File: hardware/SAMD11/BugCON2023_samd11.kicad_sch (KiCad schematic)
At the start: 26 parts, among them J1 Conn_01x04_Pin, J2 Conn_01x04_Pin, J3 Conn_01x02, P1 USB_C_Plug_USB2.0, Q1 DMG3415U-7, SW1 SW_Push, SW2 ON, U1 ATSAMD11C14A-SS, U2 AP2112K-3.3

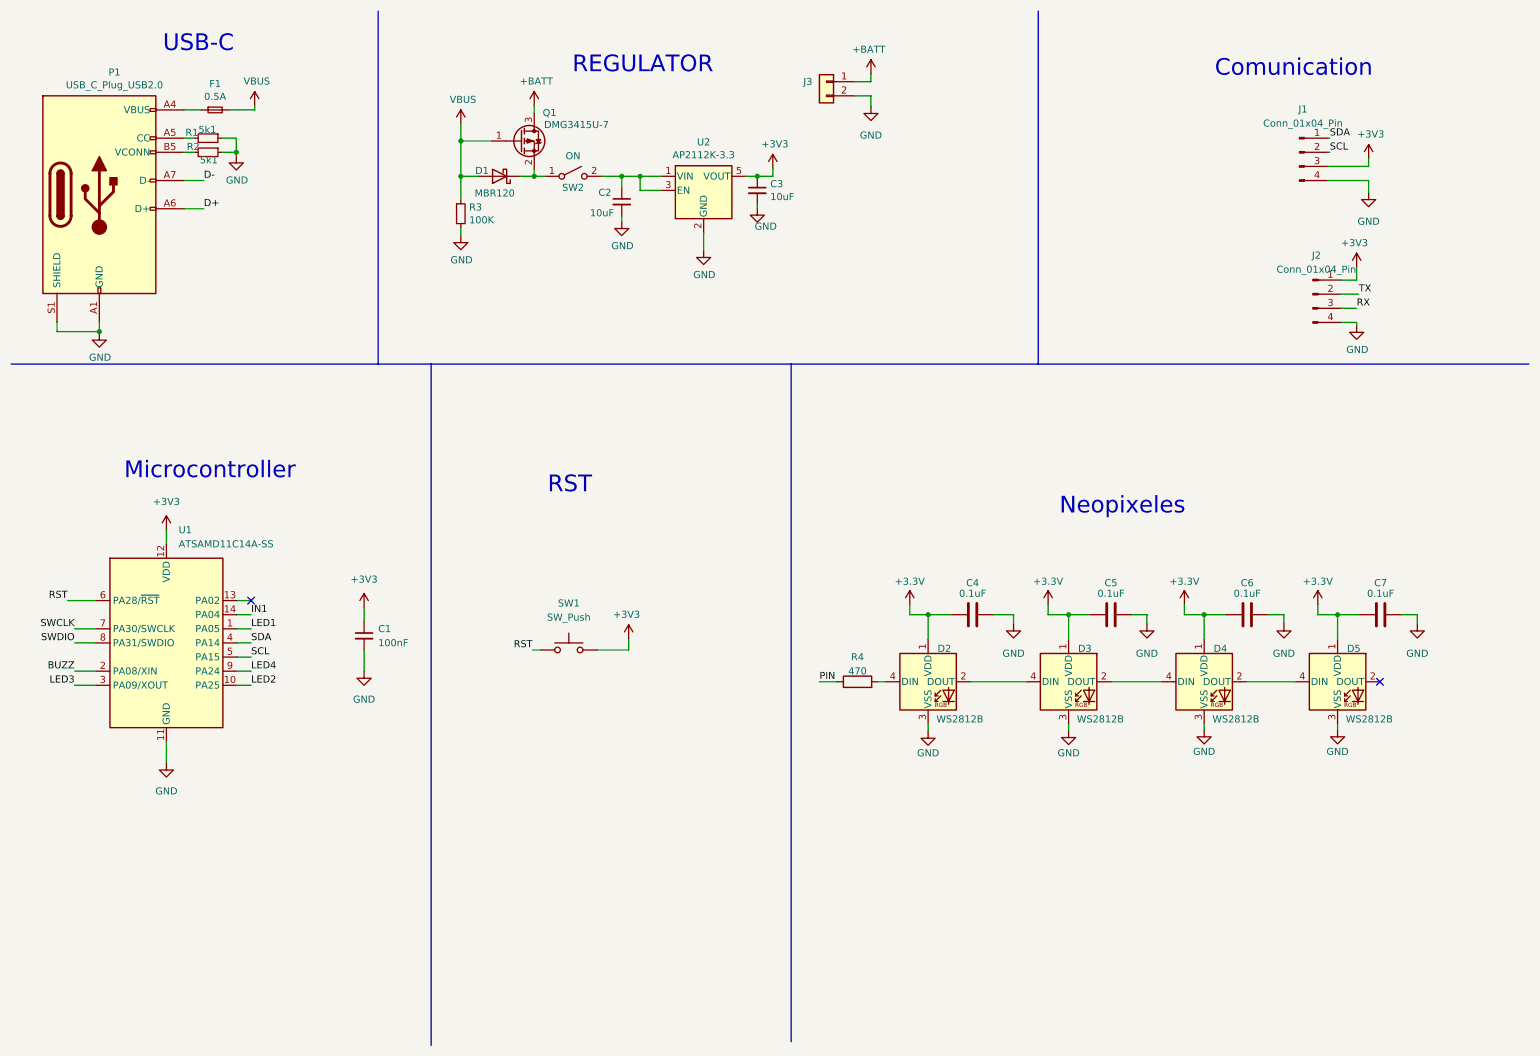
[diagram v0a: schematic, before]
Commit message: add pcb size, footprints & 3D
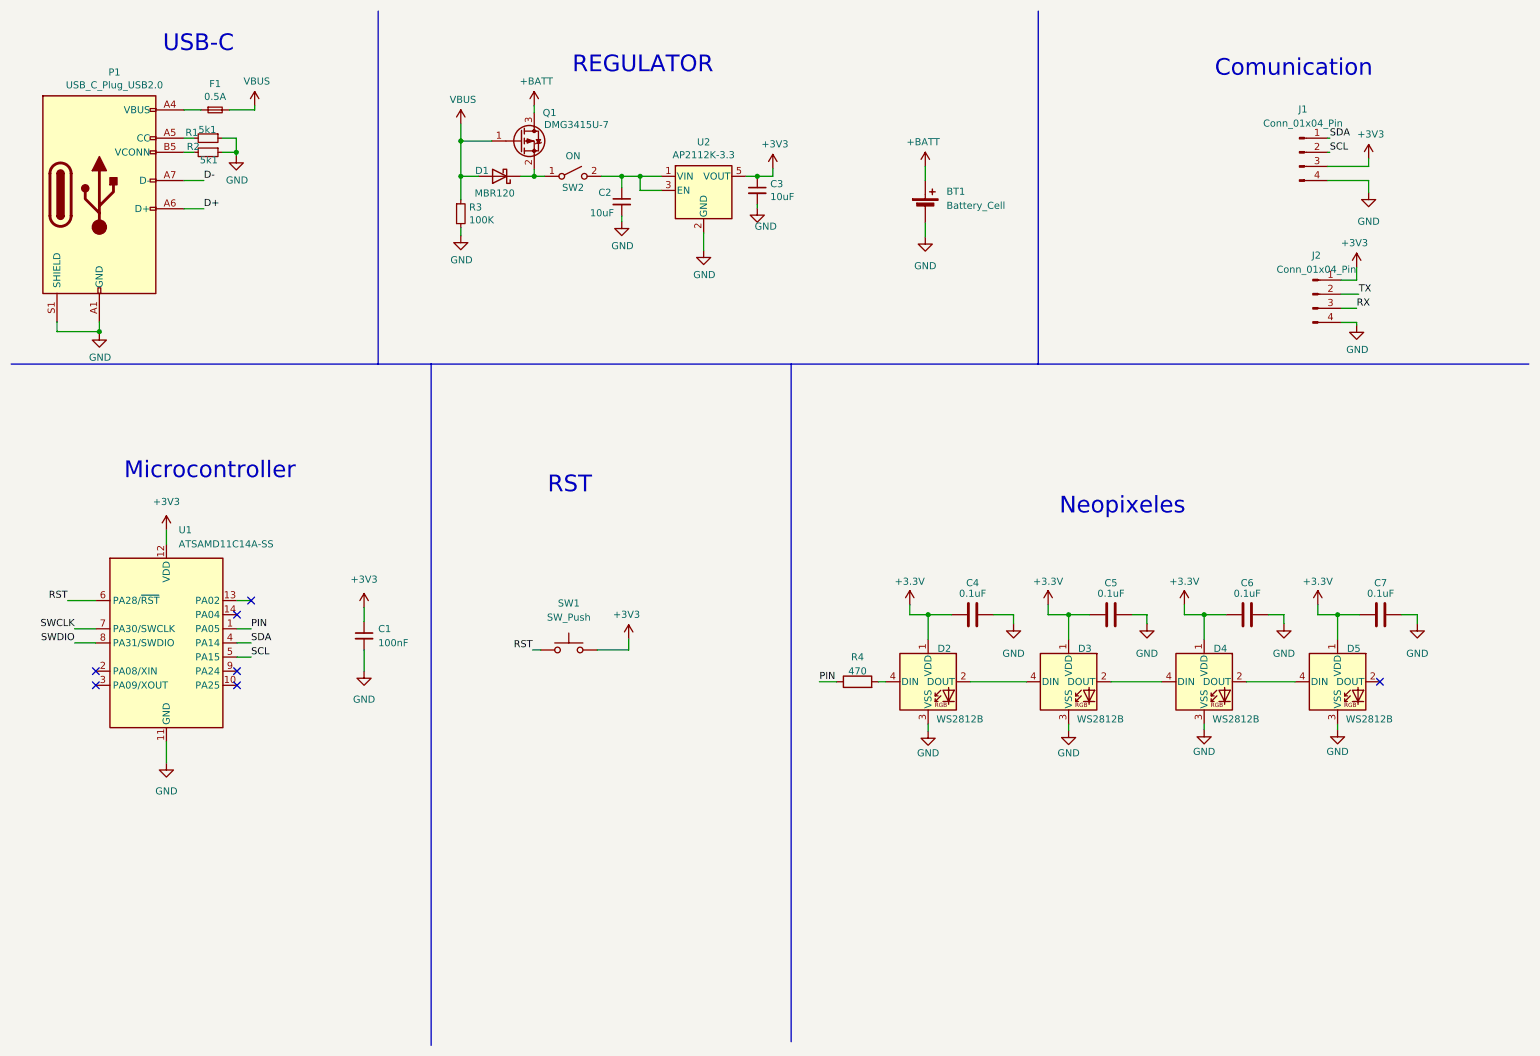
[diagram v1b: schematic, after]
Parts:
- removed J3: Conn_01x02, Connector_PinSocket_2.54mm:PinSocket_1x02_P2.54mm_Vertical, symbol Connector_Generic:Conn_01x02
- added BT1: Battery_Cell, symbol Device:Battery_Cell
- D2, D3, D4, D5: footprint FootprintsB:WS2812B_WDS -> BugCON2023_samd11:LED-SMD_4P-L3.5-W3.5-TL_WS2812B
- P1: footprint Connector_USB:USB_C_Receptacle_G-Switch_GT-USB-7010ASV -> BugCON2023_samd11:C393939
- SW2: footprint FootprintsB:SW-TH_SK12D07VG4 -> BugCON2023_samd11:JS102011SAQN; LCSC# C393937 -> C221660; manf# (none) -> JS102011SAQN
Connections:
- net LED1 is gone; now on net PIN: U1.1 (PA05)
- net +BATT: now also BT1.1 (+)
- net GND: now also BT1.2 (-)
- net BUZZ: no longer names the net of U1.2 (PA08/XIN)
- net IN1: no longer names the net of U1.14 (PA04)
- net LED2: no longer names the net of U1.10 (PA25)
- net LED3: no longer names the net of U1.3 (PA09/XOUT)
- net LED4: no longer names the net of U1.9 (PA24)
- no-connect marks 2 -> 7

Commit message: add pins of usb on samd11
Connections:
- net D+: now also U1.10 (PA25)
- net D-: now also U1.9 (PA24)
- no-connect marks 7 -> 5
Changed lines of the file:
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@@
   (junction (at 92.329 35.433) (diameter 0) (color 0 0 0 0)
   )
-  (no_connect (at 52.07 133.35))
-  (no_connect (at 52.07 130.81))
   (no_connect (at 26.67 133.35))
   (no_connect (at 26.67 130.81))
@@
     (stroke (width 0) (type default))
   )
+  (wire (pts (xy 54.61 130.81) (xy 52.07 130.81))
+    (stroke (width 0) (type default))
+  )
   (wire (pts (xy 27.305 69.723) (xy 27.305 69.977))
     (stroke (width 0) (type default))
@@
     (stroke (width 0) (type default))
   )
+  (wire (pts (xy 54.61 133.35) (xy 52.07 133.35))
+    (stroke (width 0) (type default))
+  )
   (wire (pts (xy 117.602 41.783) (xy 121.285 41.783))
     (stroke (width 0) (type default))
@@
   )
   (label "SDA" (at 54.61 125.73 0) (fields_autoplaced)
+    (effects (font (size 1.27 1.27)) (justify left bottom))
+  )
+  (label "D-" (at 54.61 130.81 0) (fields_autoplaced)
     (effects (font (size 1.27 1.27)) (justify left bottom))
   )
@@
     (effects (font (size 1.27 1.27)) (justify left bottom))
   )
+  (label "D+" (at 54.61 133.35 0) (fields_autoplaced)
+    (effects (font (size 1.27 1.27)) (justify left bottom))
+  )

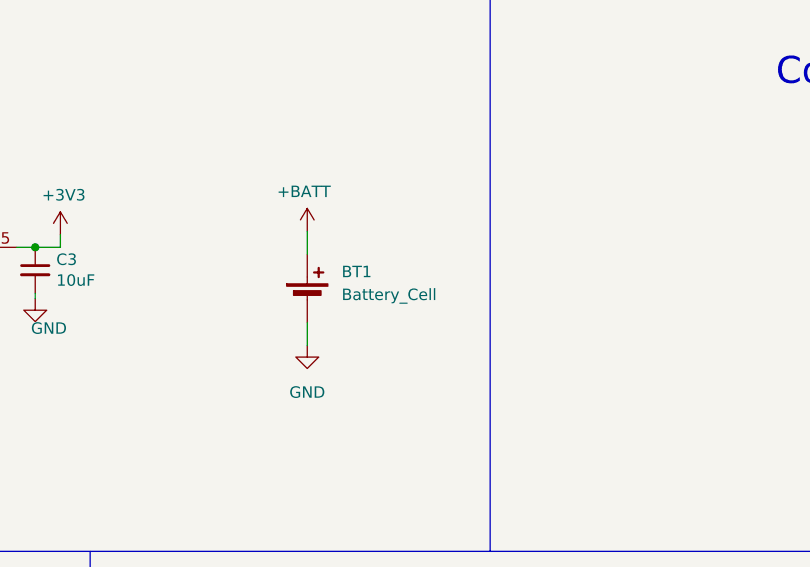
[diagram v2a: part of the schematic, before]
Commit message: add floorplan to samd11
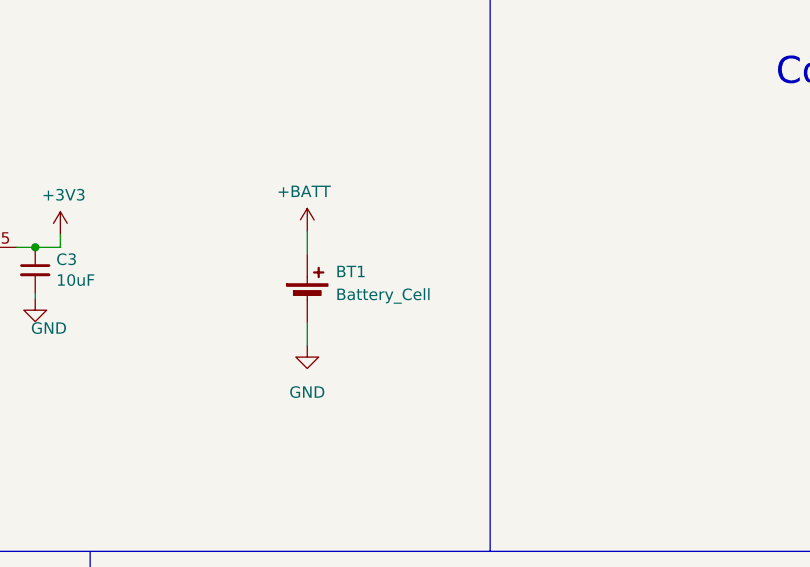
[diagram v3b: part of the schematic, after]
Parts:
- BT1: footprint (none) -> BugCON2023_samd11:BATHLD001THM
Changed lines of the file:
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@@
   (symbol (lib_id "Device:Battery_Cell") (at 175.895 47.625 0) (unit 1)
     (in_bom yes) (on_board yes) (dnp no) (fields_autoplaced)
-    (property "Reference" "BT1" (at 179.705 44.5135 0)
+    (property "Reference" "BT1" (at 179.07 44.5135 0)
       (effects (font (size 1.27 1.27)) (justify left))
     )
-    (property "Value" "Battery_Cell" (at 179.705 47.0535 0)
+    (property "Value" "Battery_Cell" (at 179.07 47.0535 0)
       (effects (font (size 1.27 1.27)) (justify left))
     )
-    (property "Footprint" "" (at 175.895 46.101 90)
+    (property "Footprint" "BugCON2023_samd11:BATHLD001THM" (at 175.895 46.101 90)
       (effects (font (size 1.27 1.27)) hide)
     )

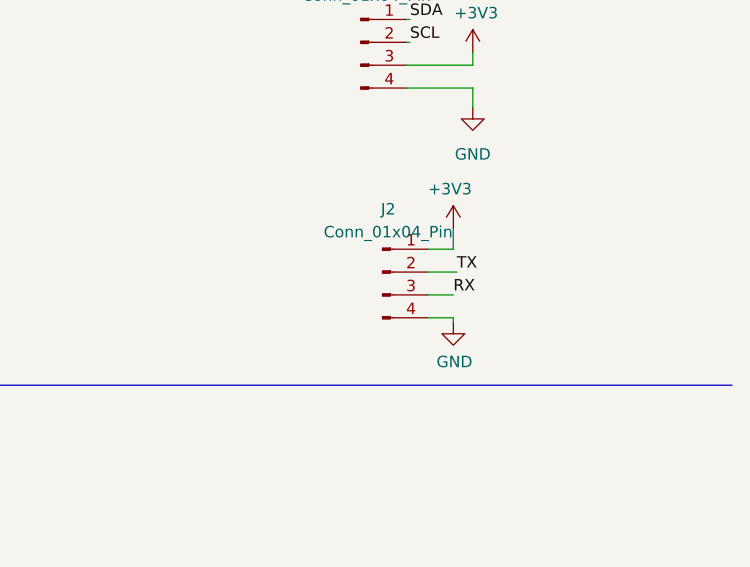
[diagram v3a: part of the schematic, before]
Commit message: upd BOM on Samd11 badge
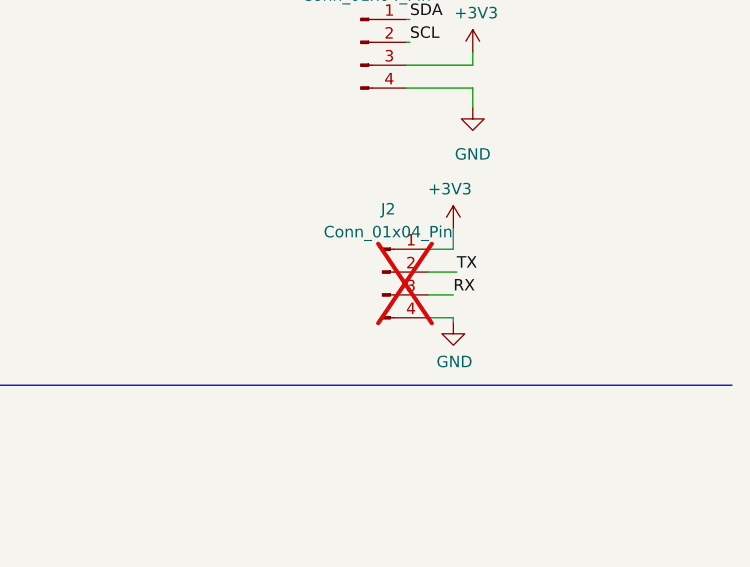
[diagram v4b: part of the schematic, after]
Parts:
- BT1: footprint BugCON2023_samd11:BATHLD001THM -> BugCON2023_samd11:BAT_12BH331P-GR; Proveedor (none) -> MOUSER; manf# (none) -> 12BH331P-GR
- C1: LCSC# (none) -> C1591; Proveedor Digikey -> LCSC
- C2, C3: Proveedor (none) -> LCSC; manf# (none) -> CL10A106MP8NNNC; provedor LCSC -> (none)
- C4, C5, C6, C7: Proveedor (none) -> LCSC; manf# (none) -> 0603F104M500NT
- D1, Q1, R1, R2: Proveedor (none) -> LCSC; provedor LCSC -> (none)
- D2, D3, D4, D5: Proveedor (none) -> LCSC; manf# (none) -> WS2812B-Mini
- F1: LCSC# - -> (none); Proveedor (none) -> MOUSER; provedor MOUSER -> (none)
- J1: Proveedor (none) -> Unit Electronics
- J2: now not fitted
- P1: LCSC# C2760486 -> C2765186; Proveedor (none) -> LCSC; manf# TYPE-C-31-M-31 -> TYPE-C 16PIN 2MD(073); provedor LCSC -> (none)
- R3: Proveedor (none) -> LCSC; manf# WR06X104JTL -> 0603WAJ0104T5E; provedor LCSC -> (none)
- R4: Proveedor (none) -> LCSC; manf# (none) -> RTT03471JTP
- SW1: LCSC# (none) -> C318889; Proveedor Digikey -> LCSC; manf# TL3342F160QG/TR -> TS-1187A-C-C-B
- SW2: footprint BugCON2023_samd11:JS102011SAQN -> BugCON2023_samd11:SW-TH_SK12D07VG4; LCSC# C221660 -> C393937; Proveedor (none) -> LCSC; manf# JS102011SAQN -> SK12D07VG4; provedor LCSC -> (none)
- U1: Proveedor Digikey -> MOUSER
- U2: LCSC# C150742 -> C51118; Proveedor (none) -> LCSC; manf# AP7365-33WG-7 -> AP2112K-3.3TRG1; provedor LCSC -> (none)

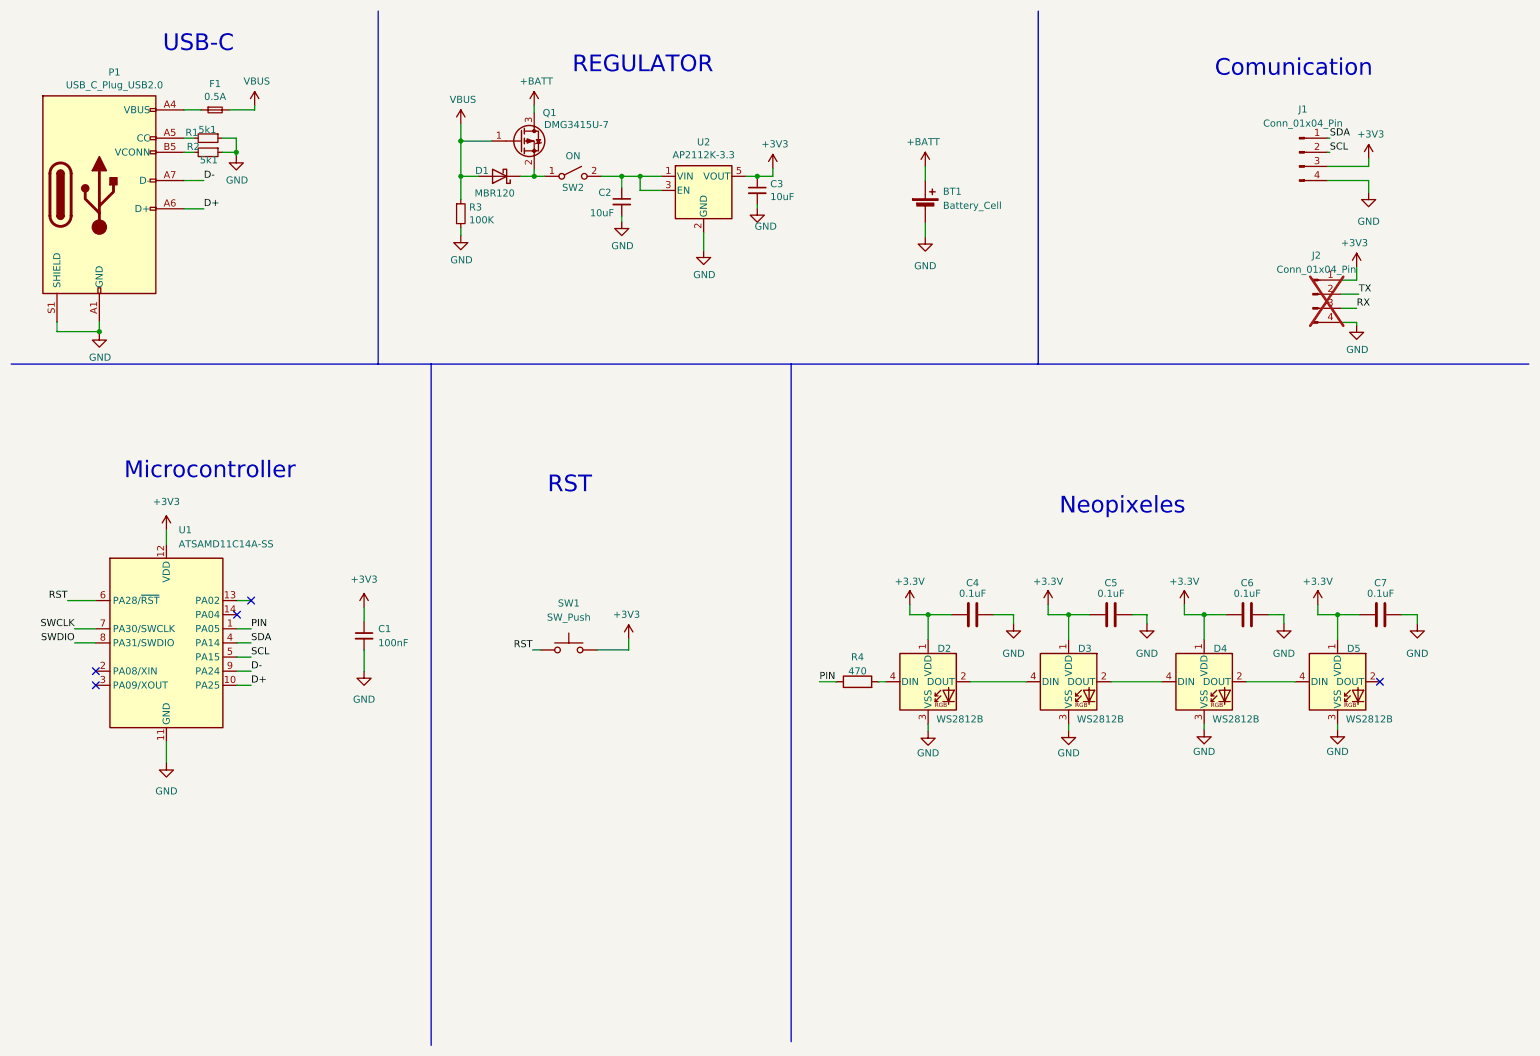
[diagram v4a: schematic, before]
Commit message: change battery connector
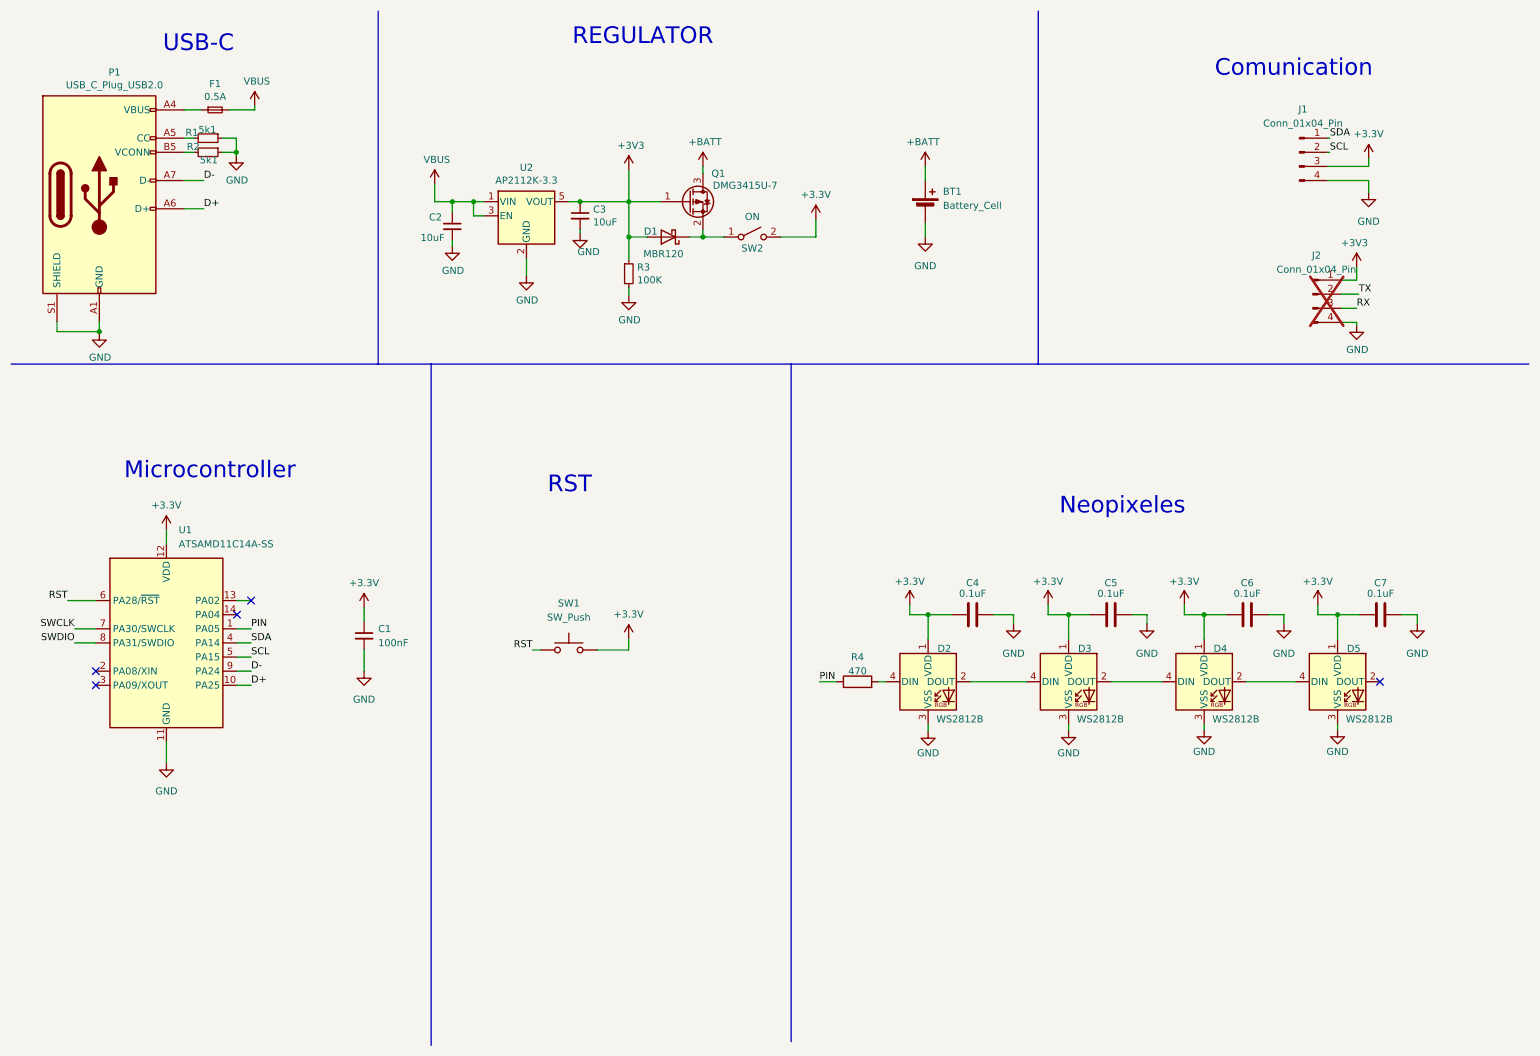
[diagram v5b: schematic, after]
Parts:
- BT1: footprint BugCON2023_samd11:BAT_12BH331P-GR -> BugCON2023_samd11:BAT_2462; manf# 12BH331P-GR -> 2462
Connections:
- net +3.3V: now also C1.1, J1.3 (Pin_3), SW1.1, SW2.2 (B), U1.12 (VDD)
- net +3V3: now also D1.2 (A), Q1.1 (G), R3.1; no longer C1.1, J1.3 (Pin_3), SW1.1, U1.12 (VDD)
- net VBUS: now also C2.1, U2.1 (VIN), U2.3 (EN); no longer D1.2 (A), Q1.1 (G), R3.1
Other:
- moved on the sheet: C2, C3, U2

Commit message: upd routing and pad connector on samd11
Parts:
- added J3: PAD2, BugCON2023_samd11:Piad, symbol Connector:Conn_01x01_Pin
- added J4: PAD, BugCON2023_samd11:Piad, symbol Connector:Conn_01x01_Pin
- added R5, R6: 4.7, Resistor_SMD:R_0603_1608Metric, symbol Device:R_Small
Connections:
- net +3.3V: now also J2.1 (Pin_1), R5.2, R6.1; no longer SW1.1
- net +3V3: no longer J2.1 (Pin_1)
- net GND: now also SW1.1
- net SCL: now also R5.1
- net SDA: now also R6.2
- net IN2: now reaches U1.13 (PA02)
- net IN2: now also J3.1 (Pin_1)
- net IN1: now reaches U1.14 (PA04)
- net IN1: now also J4.1 (Pin_1)
- no-connect marks 5 -> 3
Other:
- note added: "PAD"
